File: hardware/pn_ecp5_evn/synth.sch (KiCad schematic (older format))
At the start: 32 parts, among them J201 Conn_Coaxial, U201 VEMI65AB-HCI, U202 LMX2594

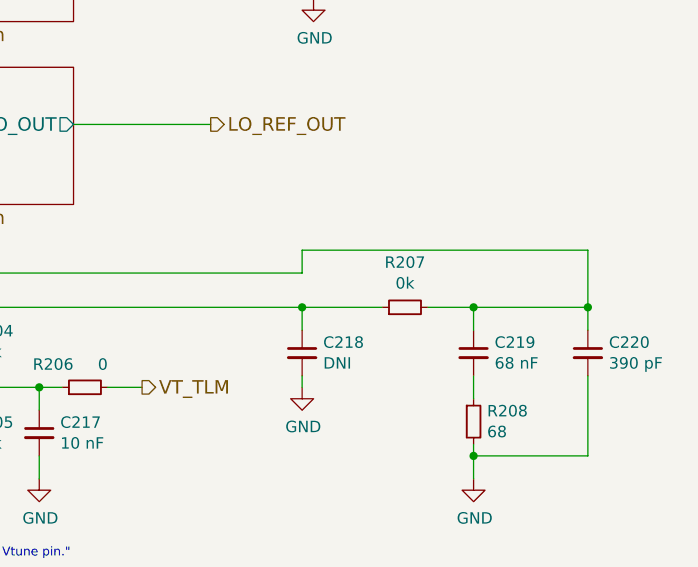
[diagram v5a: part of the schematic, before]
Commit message: added part numbers to schematic of phase noise downconverter, ordered
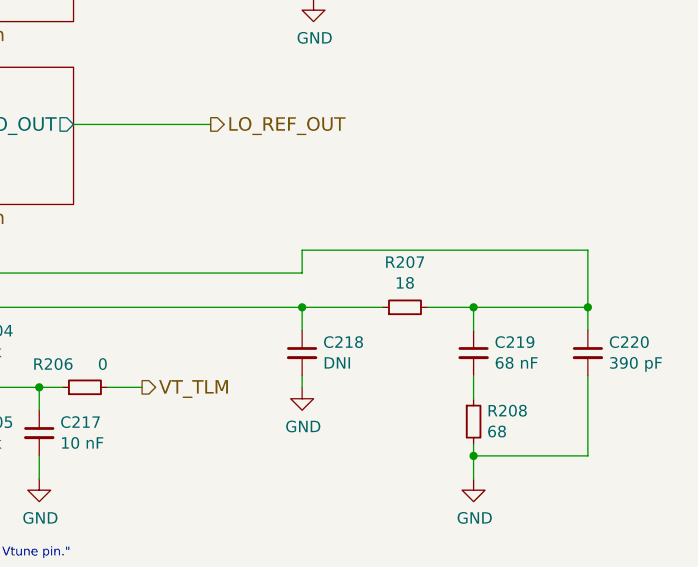
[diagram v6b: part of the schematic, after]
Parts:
- C201, C202, C203, C204, C205, C206, C207, C208, C209, C210, C211, C212, C213, C214, C216, C217, C218, D201, R201, R204, R205, R208: Distributor Part Number (none) -> N/A
- C215: Distributor Part Number (none) -> 399-17370-1-ND
- C219: Distributor Part Number (none) -> 478-10359-1-ND
- C220: Distributor Part Number (none) -> 399-1069-1-ND
- J201: Distributor (none) -> Digi-Key; Distributor Part Number (none) -> WM5534-ND
- R202: Distributor (none) -> Digi-Key; Distributor Part Number (none) -> RR05R49.9DCT-ND
- R203, R206: Distributor (none) -> Digi-Key; Distributor Part Number (none) -> P0.0JCT-ND
- R207: value 0k -> 18; Distributor Part Number (none) -> N/A
- U201: Distributor (none) -> Digi-Key; Distributor Part Number (none) -> VEMI65AB-HGS08GICT-ND
- U202: Distributor (none) -> Digi-Key; Distributor Part Number (none) -> 296-46560-1-ND
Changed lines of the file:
@@
 F 2 "Package_DFN_QFN:Texas_S-PVQFN-N40_EP4.6x4.6mm" H 5250 6050 50  0001 C CNN
 F 3 "https://www.ti.com/lit/ds/symlink/lmx2594.pdf" H 5300 4150 50  0001 C CNN
+F 4 "Digi-Key" H 5300 4150 50  0001 C CNN "Distributor"
+F 5 "296-46560-1-ND " H 5300 4150 50  0001 C CNN "Distributor Part Number"
 	1    5300 4150
 	1    0    0    -1
@@
 F 2 "Capacitor_SMD:C_0402_1005Metric" H 6500 2100 50  0001 C CNN
 F 3 "~" H 6500 2100 50  0001 C CNN
+F 4 "N/A" H 6500 2100 50  0001 C CNN "Distributor Part Number"
 	1    6500 2100
 	1    0    0    -1
@@
 F 2 "Capacitor_SMD:C_0603_1608Metric" H 3900 5300 50  0001 C CNN
 F 3 "~" H 3900 5300 50  0001 C CNN
+F 4 "N/A" H 3900 5300 50  0001 C CNN "Distributor Part Number"
 	1    3900 5300
 	1    0    0    -1
@@
 F 2 "Capacitor_SMD:C_0603_1608Metric" H 3500 5300 50  0001 C CNN
 F 3 "~" H 3500 5300 50  0001 C CNN
+F 4 "N/A" H 3500 5300 50  0001 C CNN "Distributor Part Number"
 	1    3500 5300
 	1    0    0    -1
@@
 F 2 "Capacitor_SMD:C_0402_1005Metric" H 3100 5300 50  0001 C CNN
 F 3 "~" H 3100 5300 50  0001 C CNN
+F 4 "N/A" H 3100 5300 50  0001 C CNN "Distributor Part Number"
 	1    3100 5300
 	1    0    0    -1
@@
 F 2 "Capacitor_SMD:C_0402_1005Metric" H 2700 5300 50  0001 C CNN
 F 3 "~" H 2700 5300 50  0001 C CNN
+F 4 "N/A" H 2700 5300 50  0001 C CNN "Distributor Part Number"
 	1    2700 5300
 	1    0    0    -1
@@
 F 2 "Capacitor_SMD:C_0603_1608Metric" H 2300 5300 50  0001 C CNN
 F 3 "~" H 2300 5300 50  0001 C CNN
+F 4 "N/A" H 2300 5300 50  0001 C CNN "Distributor Part Number"
 	1    2300 5300
 	1    0    0    -1
@@
 F 2 "Capacitor_SMD:C_0402_1005Metric" H 1900 5300 50  0001 C CNN
 F 3 "~" H 1900 5300 50  0001 C CNN
+F 4 "N/A" H 1900 5300 50  0001 C CNN "Distributor Part Number"
 	1    1900 5300
 	1    0    0    -1
@@
 F 2 "Capacitor_SMD:C_0603_1608Metric" H 1500 5300 50  0001 C CNN
 F 3 "~" H 1500 5300 50  0001 C CNN
+F 4 "N/A" H 1500 5300 50  0001 C CNN "Distributor Part Number"
 	1    1500 5300
 	1    0    0    -1
@@
 F 2 "Capacitor_SMD:C_0402_1005Metric" H 6850 2100 50  0001 C CNN
 F 3 "~" H 6850 2100 50  0001 C CNN
+F 4 "N/A" H 6850 2100 50  0001 C CNN "Distributor Part Number"
 	1    6850 2100
 	1    0    0    -1
@@
 F 2 "Capacitor_SMD:C_0402_1005Metric" H 6050 2100 50  0001 C CNN
 F 3 "~" H 6050 2100 50  0001 C CNN
+F 4 "N/A" H 6050 2100 50  0001 C CNN "Distributor Part Number"
 	1    6050 2100
 	1    0    0    -1
@@
 F 2 "Capacitor_SMD:C_0402_1005Metric" H 4100 2100 50  0001 C CNN
 F 3 "~" H 4100 2100 50  0001 C CNN
+F 4 "N/A" H 4100 2100 50  0001 C CNN "Distributor Part Number"
 	1    4100 2100
 	1    0    0    -1
@@
 F 2 "Capacitor_SMD:C_0402_1005Metric" H 4450 2100 50  0001 C CNN
 F 3 "~" H 4450 2100 50  0001 C CNN
+F 4 "N/A" H 4450 2100 50  0001 C CNN "Distributor Part Number"
 	1    4450 2100
 	1    0    0    -1
@@
 F 2 "Capacitor_SMD:C_0402_1005Metric" H 3750 2100 50  0001 C CNN
 F 3 "~" H 3750 2100 50  0001 C CNN
+F 4 "N/A" H 3750 2100 50  0001 C CNN "Distributor Part Number"
 	1    3750 2100
 	1    0    0    -1
@@
 F 2 "Capacitor_SMD:C_0402_1005Metric" H 3500 4100 50  0001 C CNN
 F 3 "~" H 3500 4100 50  0001 C CNN
+F 4 "N/A" H 3500 4100 50  0001 C CNN "Distributor Part Number"
 	1    3500 4100
 	0    1    1    0
@@
 F 2 "Capacitor_SMD:C_0402_1005Metric" H 3500 4250 50  0001 C CNN
 F 3 "~" H 3500 4250 50  0001 C CNN
+F 4 "N/A" H 3500 4250 50  0001 C CNN "Distributor Part Number"
 	1    3500 4250
 	0    1    1    0
@@
 F 2 "Resistor_SMD:R_0402_1005Metric" H 3150 4250 50  0001 C CNN
 F 3 "~" H 3150 4250 50  0001 C CNN
+F 4 "Digi-Key" H 3150 4250 50  0001 C CNN "Distributor"
+F 5 "RR05R49.9DCT-ND" H 3150 4250 50  0001 C CNN "Distributor Part Number"
 	1    3150 4250
 	0    -1   -1   0
@@
 F 2 "vna:LLP2513-13L" H 3100 3000 50  0001 C CNN
 F 3 "" H 3100 3000 50  0001 C CNN
+F 4 "Digi-Key" H 3050 3200 50  0001 C CNN "Distributor"
+F 5 "VEMI65AB-HGS08GICT-ND" H 3050 3200 50  0001 C CNN "Distributor Part Number"
 	1    3050 3200
 	1    0    0    -1
@@
 F 2 "Resistor_SMD:R_0402_1005Metric" H 3900 3600 50  0001 C CNN
 F 3 "~" H 3900 3600 50  0001 C CNN
+F 4 "Digi-Key" H 3900 3600 50  0001 C CNN "Distributor"
+F 5 "P0.0JCT-ND " H 3900 3600 50  0001 C CNN "Distributor Part Number"
 	1    3900 3600
 	0    -1   -1   0
@@
 F 2 "Capacitor_SMD:C_0402_1005Metric" H 6600 5150 50  0001 C CNN
 F 3 "~" H 6600 5150 50  0001 C CNN
+F 4 "399-17370-1-ND " H 6600 5150 50  0001 C CNN "Distributor Part Number"
 	1    6600 5150
 	1    0    0    -1
@@
 F 2 "Capacitor_SMD:C_0603_1608Metric" H 8650 5150 50  0001 C CNN
 F 3 "~" H 8650 5150 50  0001 C CNN
+F 4 "N/A" H 8650 5150 50  0001 C CNN "Distributor Part Number"
 	1    8650 5150
 	1    0    0    -1
@@
 F 2 "Resistor_SMD:R_0402_1005Metric" H 7150 5100 50  0001 C CNN
 F 3 "~" H 7150 5100 50  0001 C CNN
+F 4 "N/A" H 7150 5100 50  0001 C CNN "Distributor Part Number"
 	1    7150 5100
 	1    0    0    -1
@@
 F 2 "Capacitor_SMD:C_0402_1005Metric" H 7500 5500 50  0001 C CNN
 F 3 "~" H 7500 5500 50  0001 C CNN
+F 4 "N/A" H 7500 5500 50  0001 C CNN "Distributor Part Number"
 	1    7500 5500
 	1    0    0    -1
@@
 F 2 "Resistor_SMD:R_0402_1005Metric" H 7150 5500 50  0001 C CNN
 F 3 "~" H 7150 5500 50  0001 C CNN
+F 4 "N/A" H 7150 5500 50  0001 C CNN "Distributor Part Number"
 	1    7150 5500
 	1    0    0    -1
@@
 P 9100 4950
 F 0 "R207" V 9296 4950 50  0000 C CNN
-F 1 "0k" V 9205 4950 50  0000 C CNN
+F 1 "18" V 9205 4950 50  0000 C CNN
 F 2 "Resistor_SMD:R_0402_1005Metric" H 9100 4950 50  0001 C CNN
 F 3 "~" H 9100 4950 50  0001 C CNN
+F 4 "N/A" H 9100 4950 50  0001 C CNN "Distributor Part Number"
 	1    9100 4950
 	0    -1   -1   0
@@
 F 2 "Capacitor_SMD:C_0603_1608Metric" H 9400 5150 50  0001 C CNN
 F 3 "~" H 9400 5150 50  0001 C CNN
+F 4 "478-10359-1-ND" H 9400 5150 50  0001 C CNN "Distributor Part Number"
 	1    9400 5150
 	1    0    0    -1
@@
 F 2 "Resistor_SMD:R_0402_1005Metric" H 9400 5450 50  0001 C CNN
 F 3 "~" H 9400 5450 50  0001 C CNN
+F 4 "N/A" H 9400 5450 50  0001 C CNN "Distributor Part Number"
 	1    9400 5450
 	1    0    0    -1
@@
 F 2 "Capacitor_SMD:C_0603_1608Metric" H 9900 5150 50  0001 C CNN
 F 3 "~" H 9900 5150 50  0001 C CNN
+F 4 "399-1069-1-ND" H 9900 5150 50  0001 C CNN "Distributor Part Number"
 	1    9900 5150
 	1    0    0    -1
@@
 F 2 "vna:SMA_Molex_73251-1153_OSHFR408" H 8700 3350 50  0001 C CNN
 F 3 " ~" H 8700 3350 50  0001 C CNN
+F 4 "WM5534-ND" H 8700 3350 50  0001 C CNN "Distributor Part Number"
+F 5 "Digi-Key" H 8700 3350 50  0001 C CNN "Distributor"
 	1    8700 3350
 	1    0    0    -1
@@
 F 2 "Resistor_SMD:R_0402_1005Metric" H 7700 5300 50  0001 C CNN
 F 3 "~" H 7700 5300 50  0001 C CNN
+F 4 "Digi-Key" H 7700 5300 50  0001 C CNN "Distributor"
+F 5 "P0.0JCT-ND " H 7700 5300 50  0001 C CNN "Distributor Part Number"
 	1    7700 5300
 	0    -1   -1   0
@@
 F 2 "LED_SMD:LED_0603_1608Metric" V 1250 3550 50  0001 C CNN
 F 3 "~" V 1250 3550 50  0001 C CNN
+F 4 "N/A" H 1250 3550 50  0001 C CNN "Distributor Part Number"
 	1    1250 3550
 	0    -1   -1   0
@@
 F 2 "Resistor_SMD:R_0402_1005Metric" H 1250 3950 50  0001 C CNN
 F 3 "~" H 1250 3950 50  0001 C CNN
+F 4 "N/A" H 1250 3950 50  0001 C CNN "Distributor Part Number"
 	1    1250 3950
 	1    0    0    -1
